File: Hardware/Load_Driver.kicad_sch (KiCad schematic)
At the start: 0 parts

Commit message: Added Relay Driver schematics
- added the ICs, relay sockets, etc
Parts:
- added J1, J2: VCF4-1000, VCF4-1000:TE_VCF4-1000, symbol symbols:VCF4-1000
- added LD1, LD2: TPL7407LA, symbol symbols:TPL7407LA
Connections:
- new net +12V: J1.30, J2.30, LD1. (OUT7), LD2. (OUT7)
- new net GND: J1.85, J2.85, LD1. (OUT7), LD2. (OUT7)
- new net HighChan1: LD1. (OUT7)
- new net HighChan2: LD2. (OUT7)
- new net HighDrive1: J1.86, LD1. (OUT7)
- new net HighDrive2: J2.86, LD2. (OUT7)
- new net HighDriveOut1: J1.87
- new net HighDriveOut2: J2.87
- new net LowChan1: LD1. (OUT7)
- new net LowChan2: LD1. (OUT7), LD2. (OUT7)
- new net LowChan3: LD2. (OUT7)
- new net LowDrive1: LD1. (OUT7)
- new net LowDrive2: LD1. (OUT7), LD2. (OUT7)
- new net LowDrive3: LD2. (OUT7)
- no-connect marks 0 -> 14
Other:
- note added: "- The load driver ICs are the recommended TPL7407LA's. - The drivers themselves have only 7 channels, from which we need 2 and have to double up on 3 more. - Thus, to split the current evenly (put equal load on both ICs), I've set one HighDrive (single channel running a relay coil) per IC, and an additional doubled up LowDrive (1.6A direct draw) per IC. Then, for the last LowDrive, I've split it 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"
- note added: "DIN 72552 Standard - 30: Common - 85: Coil Ground - 86: Coil Positive - 87: Normally Open Output - 87A: Normally Closed Output"
- note added: "Design Notes"
- note added: "Global/Hierarchical Labels"
- note added: "Load Driver ICs"
- note added: "Relay Sockets"

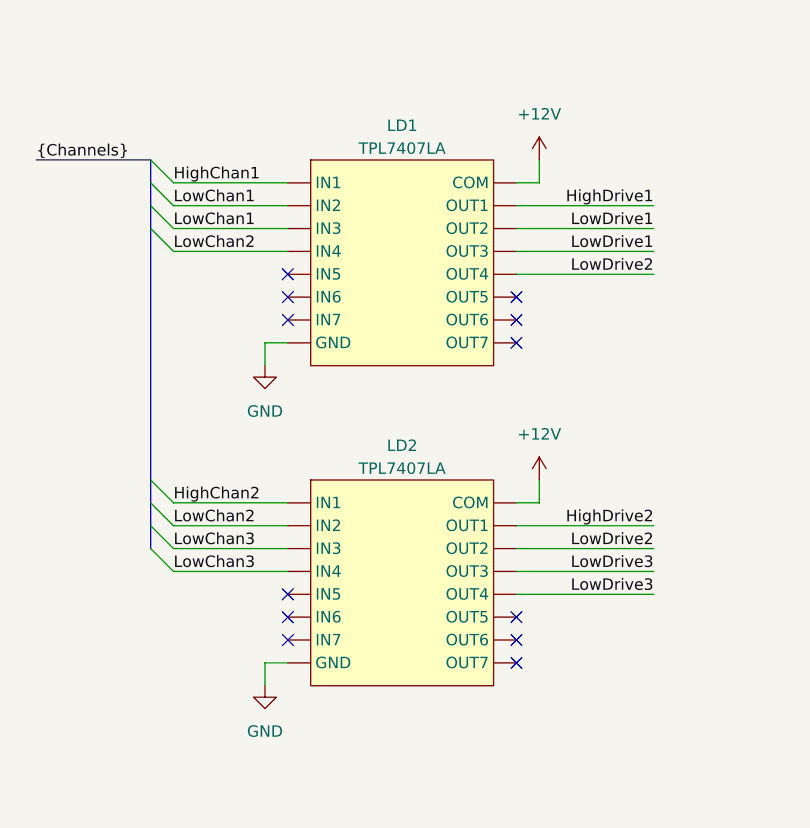
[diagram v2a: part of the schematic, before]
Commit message: Finished final touches on schematic.
- Schematic is complete (NOT yet checked by Yassa/Val)
- ERC check is complete, understandable errors excused w/ comments
- Final schematic formatting complete

Co-authored-by: Kostadin Madjovski <155325994+bivein@users.noreply.github.com>
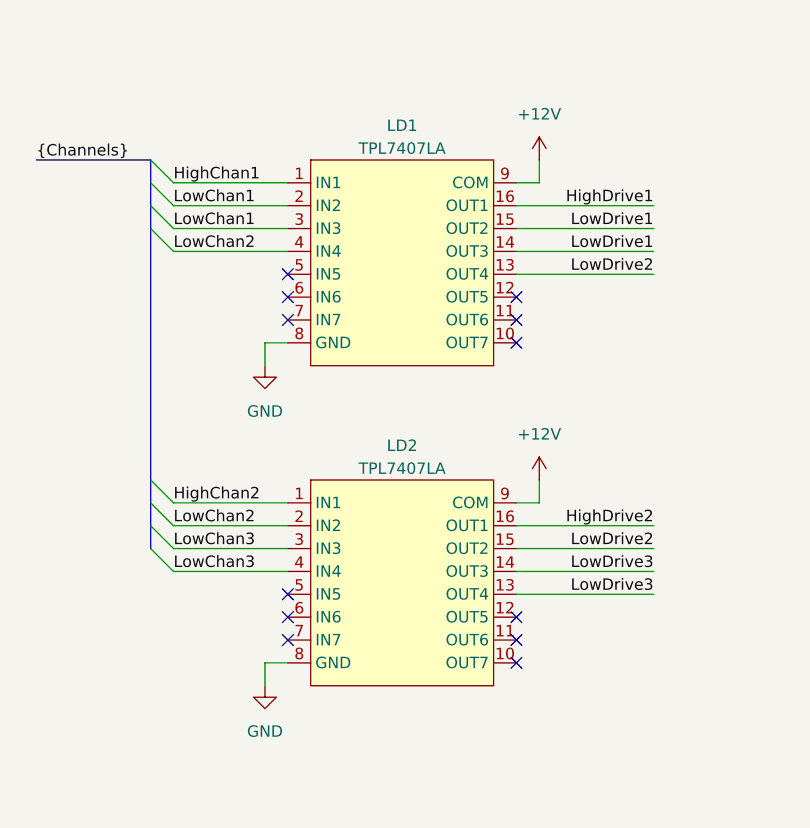
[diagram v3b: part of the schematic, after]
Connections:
- net +12V: now also LD1.9 (COM), LD2.9 (COM); no longer LD1. (OUT7), LD2. (OUT7)
- net GND: now also LD1.8 (GND), LD2.8 (GND); no longer LD1. (OUT7), LD2. (OUT7)
- net HighChan1: now also LD1.1 (IN1); no longer LD1. (OUT7)
- net HighChan2: now also LD2.1 (IN1); no longer LD2. (OUT7)
- net HighDrive1: now also LD1.16 (OUT1); no longer LD1. (OUT7)
- net HighDrive2: now also LD2.16 (OUT1); no longer LD2. (OUT7)
- net LowChan1: now also LD1.2 (IN2), LD1.3 (IN3); no longer LD1. (OUT7)
- net LowChan2: now also LD1.4 (IN4), LD2.2 (IN2); no longer LD1. (OUT7), LD2. (OUT7)
- net LowChan3: now also LD2.3 (IN3), LD2.4 (IN4); no longer LD2. (OUT7)
- net LowDrive1: now also LD1.14 (OUT3), LD1.15 (OUT2); no longer LD1. (OUT7)
- net LowDrive2: now also LD1.13 (OUT4), LD2.15 (OUT2); no longer LD1. (OUT7), LD2. (OUT7)
- net LowDrive3: now also LD2.13 (OUT4), LD2.14 (OUT3); no longer LD2. (OUT7)
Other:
- company: (none) -> NJIT Solar Car
- title: (none) -> CAN IO Board | Load Driver
